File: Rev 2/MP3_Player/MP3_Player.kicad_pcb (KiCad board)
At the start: 2 copper layers, 15.2 x 2.5 mm, 28 parts, among them J1 AudioJack3_SwitchT, M1 Haptic Feedback, Q1 BS170, SW1 Home, SW2 Back, SW3 Play/Pause, SW4 Power, SW5 Menu, SW6 Hold, U1 Wemos Lolin32 Lite

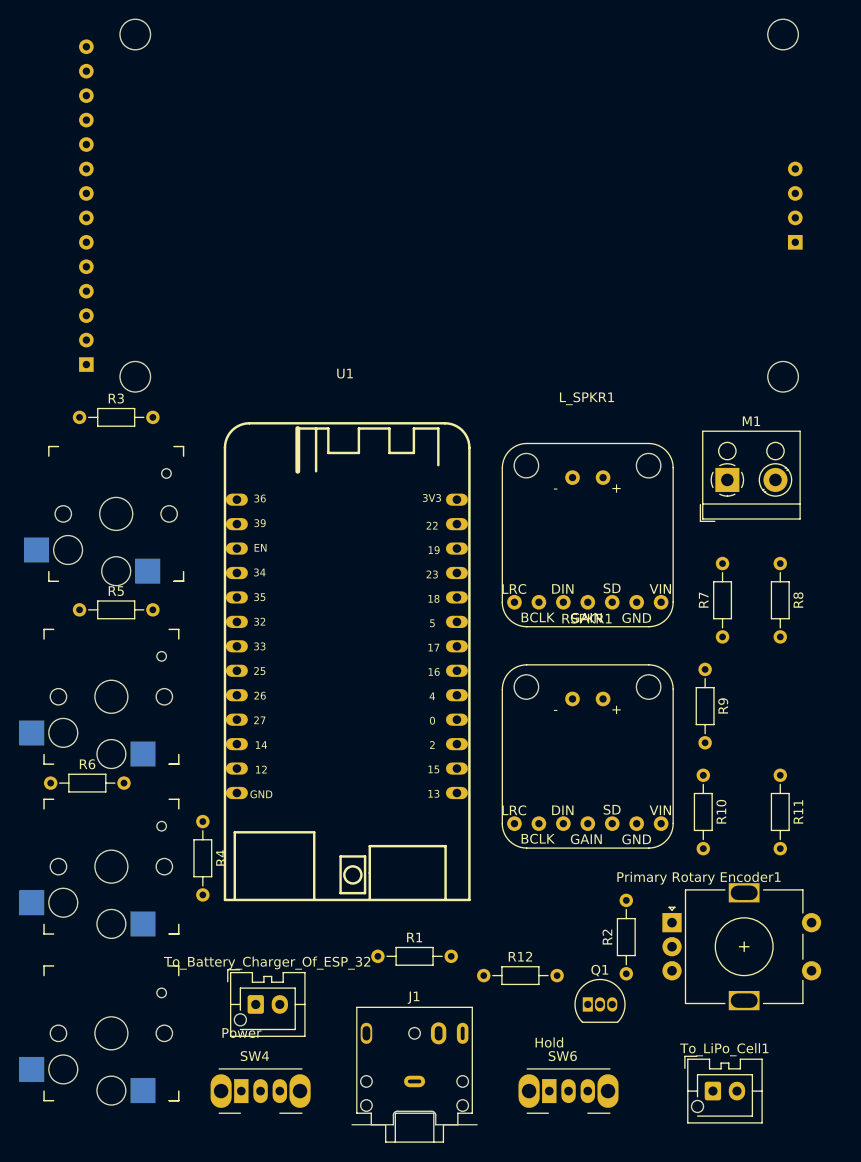
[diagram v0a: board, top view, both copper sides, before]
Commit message: wired power and ground
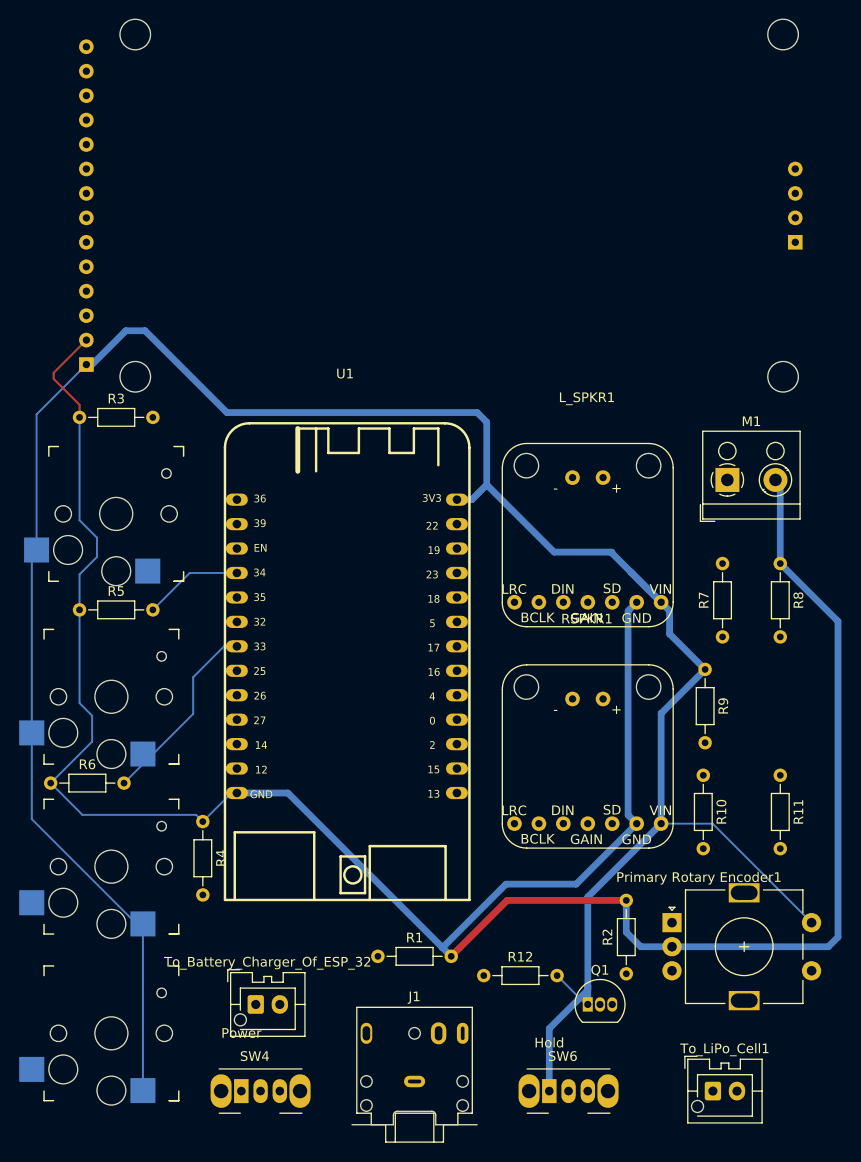
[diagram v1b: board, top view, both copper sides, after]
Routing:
- net /VDD: track 0.00 -> 253.6 mm
- net GND: track 0.00 -> 250.9 mm
- net Net-(SW2-A): track 0.00 -> 19.8 mm
- net Net-(SW5-B): track 0.00 -> 10.3 mm
